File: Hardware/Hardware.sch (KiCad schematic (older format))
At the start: 65 parts

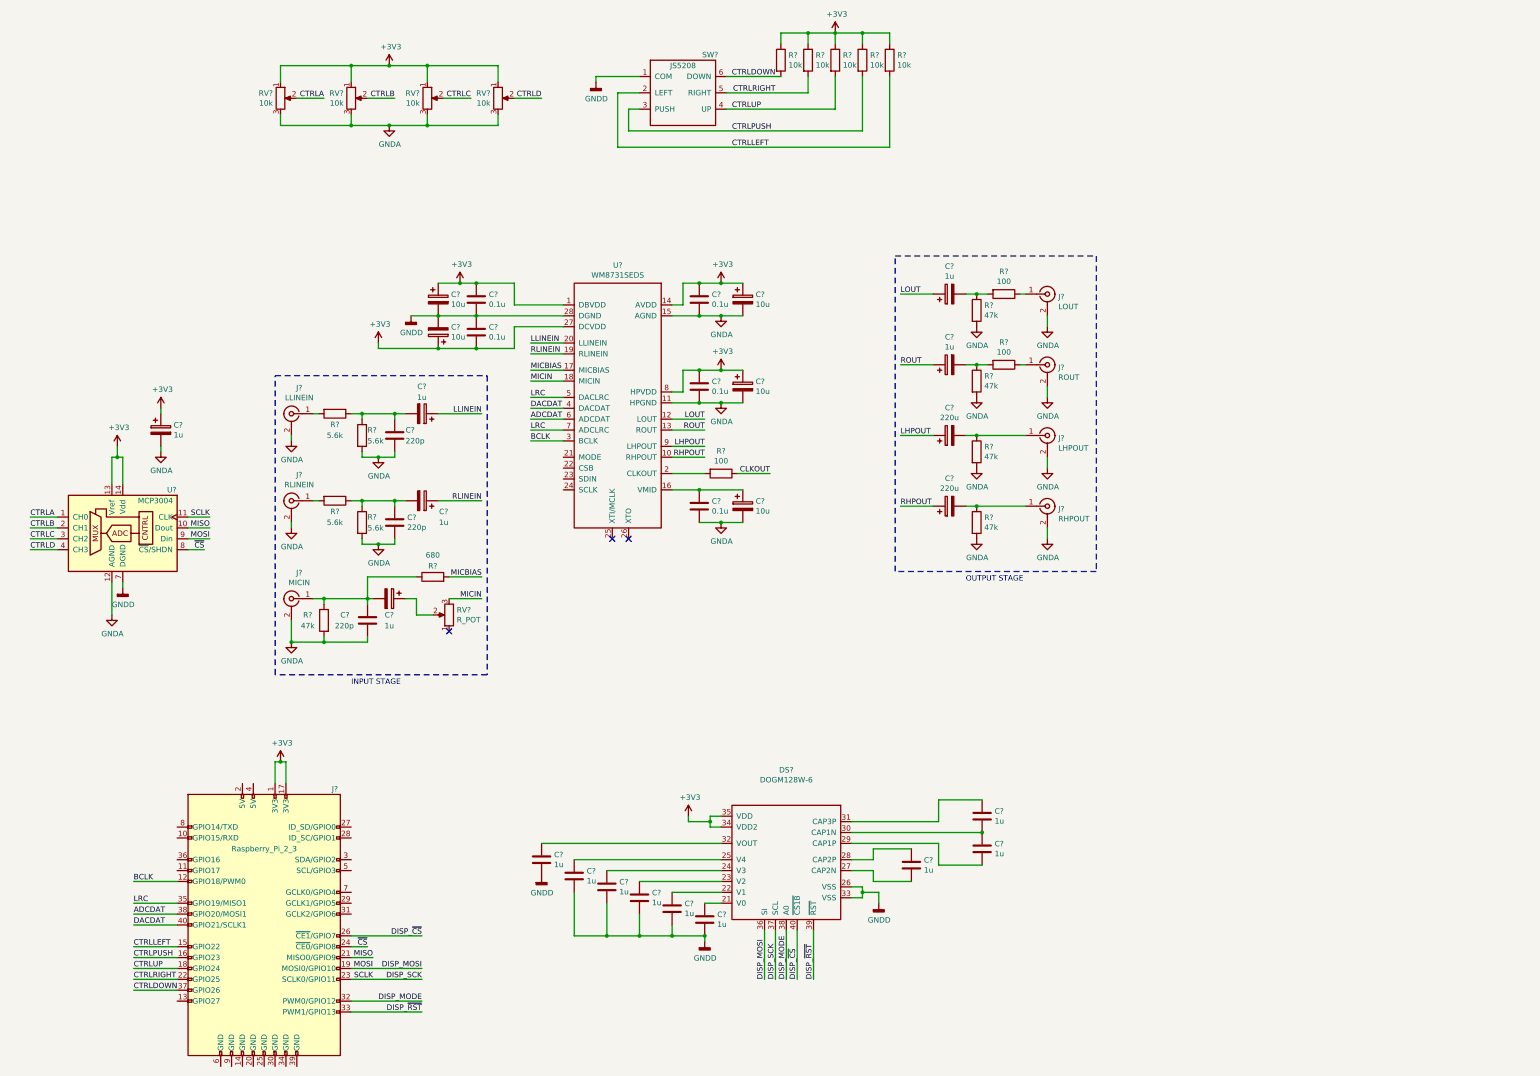
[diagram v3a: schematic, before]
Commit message: Organised schematic sheet
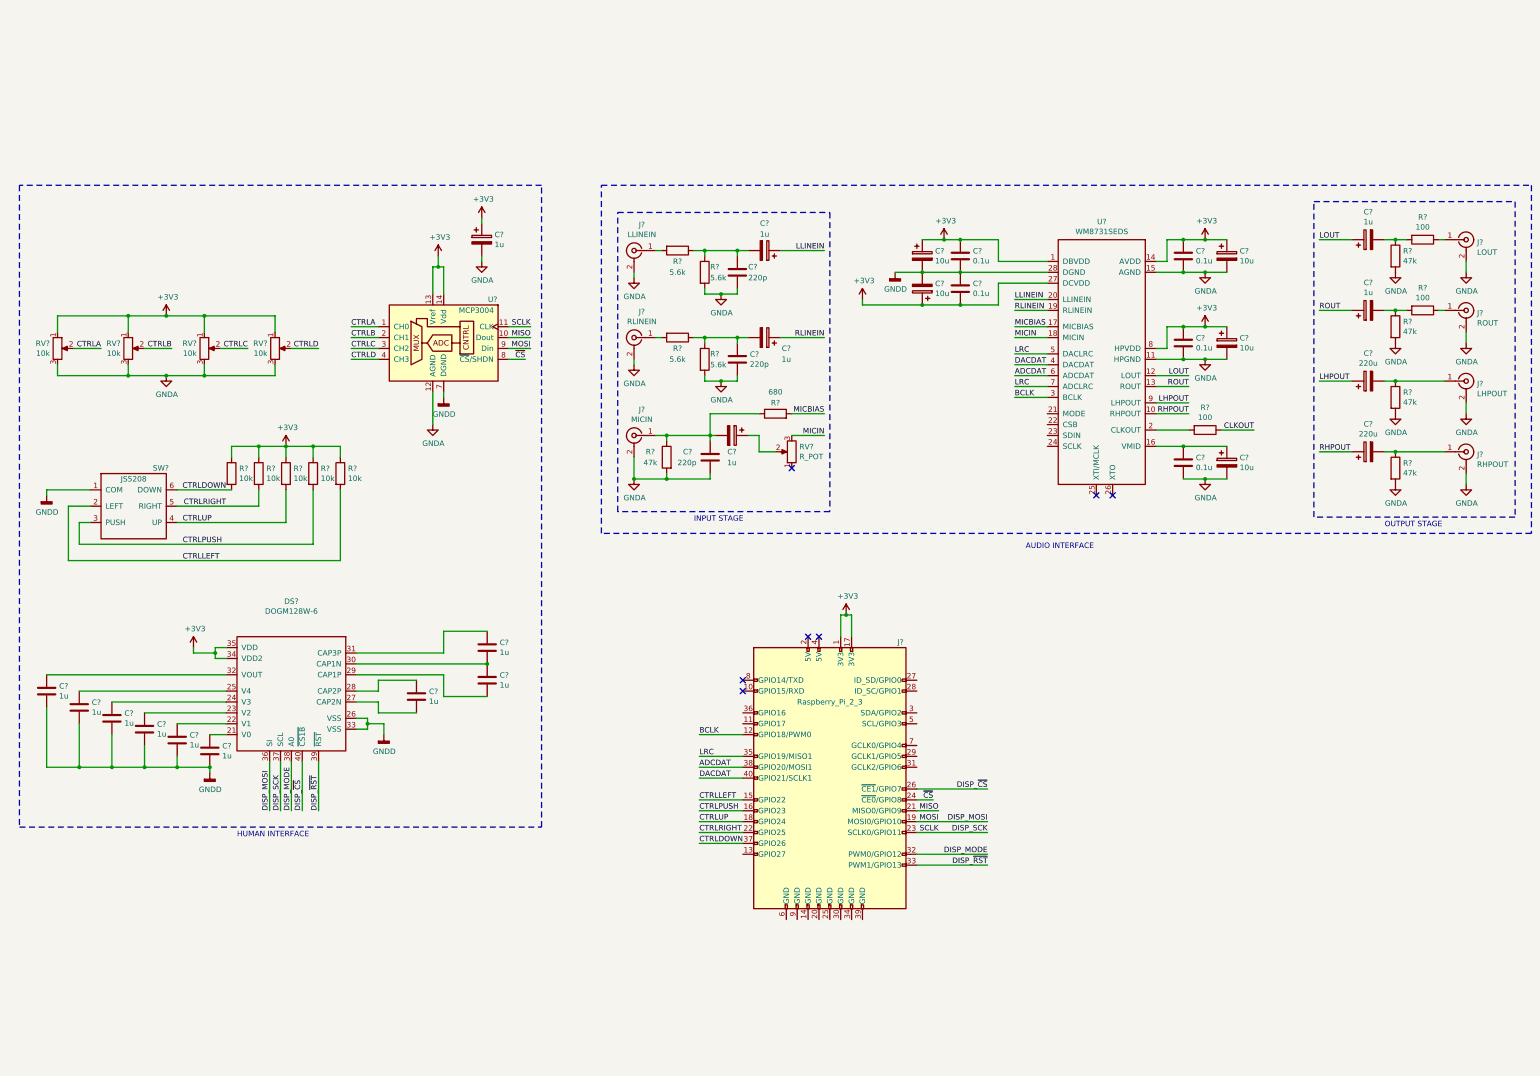
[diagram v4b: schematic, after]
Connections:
- no-connect marks 3 -> 7
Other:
- note added: "AUDIO INTERFACE"
- note added: "HUMAN INTERFACE"
- moved on the sheet: C?, DS?, J?, R?, RV?, SW?, U?

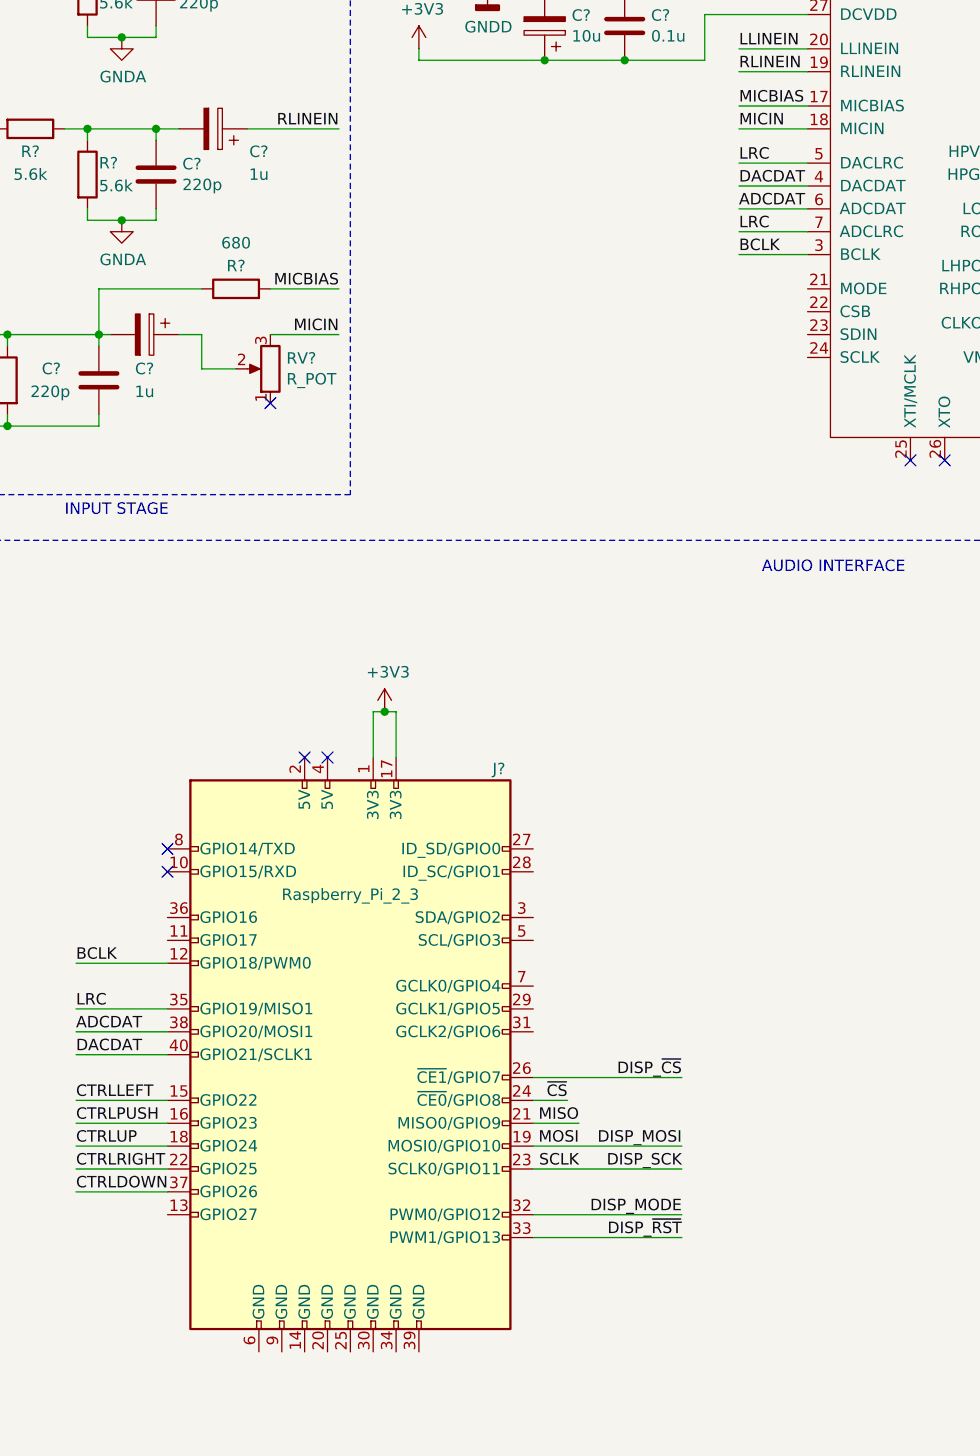
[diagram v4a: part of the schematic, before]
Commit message: Connected WM8731SEDS control interface through i2c to Raspberry Pi, finished connection of all systems
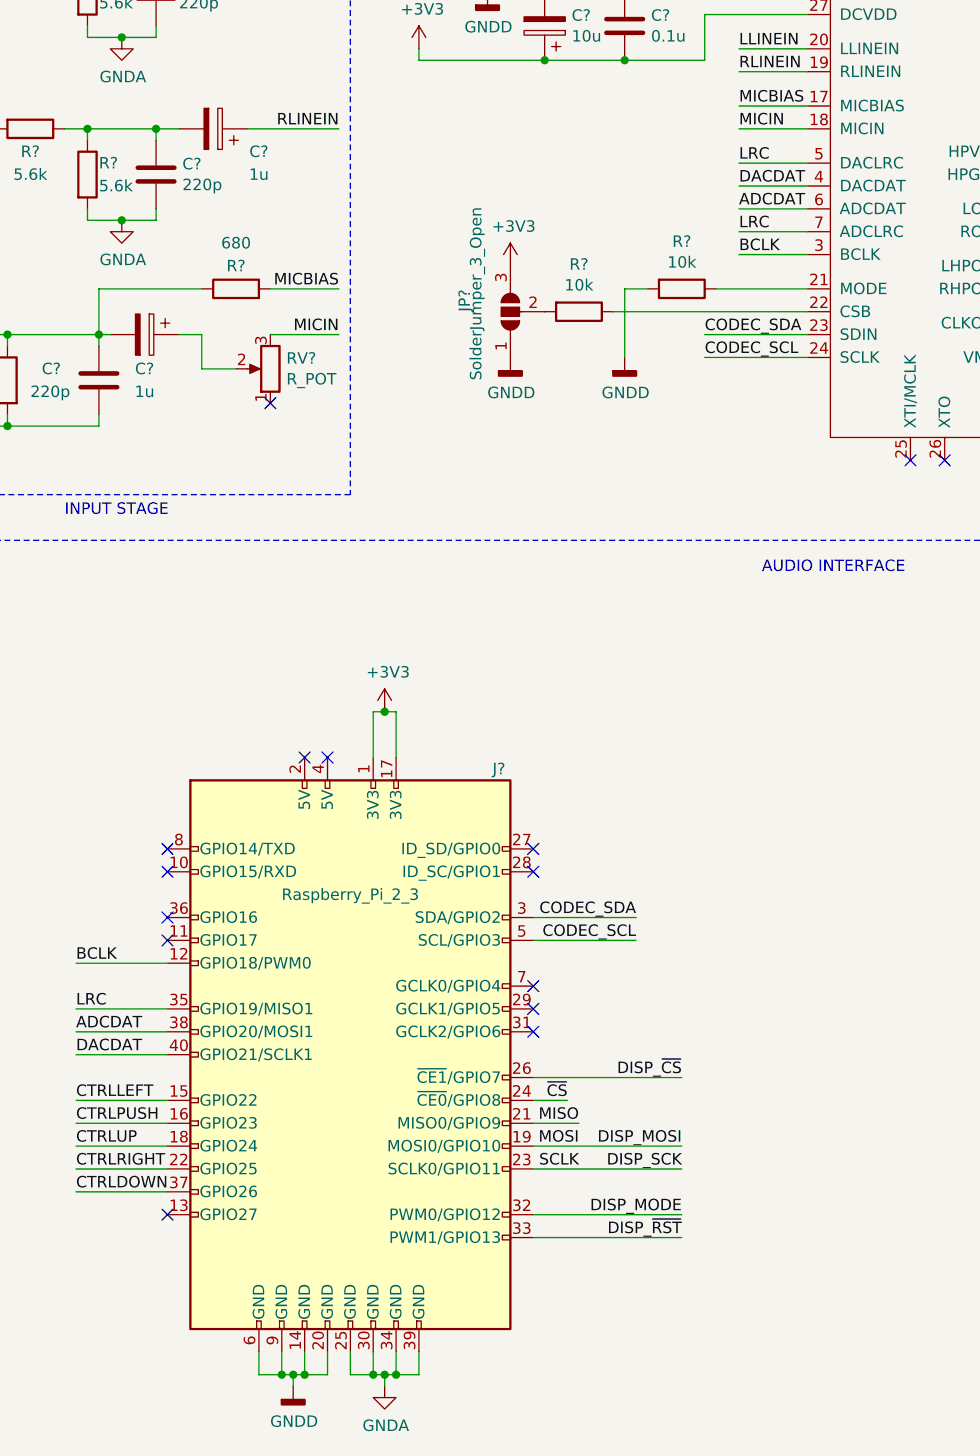
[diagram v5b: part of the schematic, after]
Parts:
- added JP?: SolderJumper_3_Open, symbol Jumper:SolderJumper_3_Open
- added R? (x2): 10k, symbol Device:R
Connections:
- net +3V3: now also JP?.3 (B)
- net GNDA: now also J?.25 (GND), J?.30 (GND), J?.34 (GND), J?.39 (GND)
- net GNDD: now also J?.14 (GND), J?.20 (GND), J?.6 (GND), J?.9 (GND), JP?.1 (A), R?.2
- net CODEC_SDA: now reaches J?.3 (SDA/GPIO2)
- net CODEC_SDA: now also U?.23 (SDIN)
- net CODEC_SCL: now reaches J?.5 (SCL/GPIO3)
- net CODEC_SCL: now also U?.24 (SCLK)
- net at U?.21 (MODE): now also R?.1
- net at U?.22 (CSB): now also R?.1
- new net: JP?.2 (C), R?.2
- no-connect marks 7 -> 15
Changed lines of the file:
@@
 encoding utf-8
 Sheet 1 1
-Title ""
-Date ""
-Rev ""
-Comp ""
+Title "signl main"
+Date "2020-02-18"
+Rev "1.0"
+Comp "signl"
 Comment1 ""
 Comment2 ""
@@
 NoConn ~ 7550 6800
 NoConn ~ 7550 6900
+$Comp
+L Device:R R?
+U 1 1 5E4D012A
+P 9350 4450
+F 0 "R?" V 9143 4450 50  0000 C CNN
+F 1 "10k" V 9234 4450 50  0000 C CNN
+F 2 "" V 9280 4450 50  0001 C CNN
+F 3 "~" H 9350 4450 50  0001 C CNN
+	1    9350 4450
+	0    1    1    0
+$EndComp
+$Comp
+L Jumper:SolderJumper_3_Open JP?
+U 1 1 5E4D0C03
+P 9050 4450
+F 0 "JP?" H 9050 4650 50  0000 L CNN
+F 1 "SolderJumper_3_Open" H 8750 4600 50  0000 L CNN
+F 2 "" H 9050 4450 50  0001 C CNN
+F 3 "~" H 9050 4450 50  0001 C CNN
+	1    9050 4450
+	0    -1   -1   0
+$EndComp
+Wire Wire Line
+	9500 4450 10350 4450
+$Comp
+L power:+3V3 #PWR?
+U 1 1 5E4E3D4A
+P 9050 4250
+F 0 "#PWR?" H 9050 4100 50  0001 C CNN
+F 1 "+3V3" H 9065 4423 50  0000 C CNN
+F 2 "" H 9050 4250 50  0001 C CNN
+F 3 "" H 9050 4250 50  0001 C CNN
+	1    9050 4250
+	1    0    0    -1
+$EndComp
+$Comp
+L power:GNDD #PWR?
+U 1 1 5E4E4370
+P 9050 4650
+F 0 "#PWR?" H 9050 4400 50  0001 C CNN
+F 1 "GNDD" H 9054 4495 50  0000 C CNN
+F 2 "" H 9050 4650 50  0001 C CNN
+F 3 "" H 9050 4650 50  0001 C CNN
+	1    9050 4650
+	1    0    0    -1
+$EndComp
+$Comp
+L Device:R R?
+U 1 1 5E4E4813
+P 9800 4350
+F 0 "R?" V 9593 4350 50  0000 C CNN
+F 1 "10k" V 9684 4350 50  0000 C CNN
+F 2 "" V 9730 4350 50  0001 C CNN
+F 3 "~" H 9800 4350 50  0001 C CNN
+	1    9800 4350
+	0    1    1    0
+$EndComp
+Wire Wire Line
+	9950 4350 10350 4350
+Wire Wire Line
+	9650 4350 9550 4350
+Wire Wire Line
+	9550 4350 9550 4650
+$Comp
+L power:GNDD #PWR?
+U 1 1 5E54E244
+P 9550 4650
+F 0 "#PWR?" H 9550 4400 50  0001 C CNN
+F 1 "GNDD" H 9554 4495 50  0000 C CNN
+F 2 "" H 9550 4650 50  0001 C CNN
+F 3 "" H 9550 4650 50  0001 C CNN
+	1    9550 4650
+	1    0    0    -1
+$EndComp
+Text Label 9900 4550 0    50   ~ 0
+CODEC_SDA
+Wire Wire Line
+	9900 4550 10350 4550
+Text Label 9900 4650 0    50   ~ 0
+CODEC_SCL
+Wire Wire Line
+	9900 4650 10350 4650
+Text Label 9600 7100 2    50   ~ 0
+CODEC_SDA
+Wire Wire Line
+	9600 7100 9150 7100
+Text Label 9600 7200 2    50   ~ 0
+CODEC_SCL
+Wire Wire Line
+	9600 7200 9150 7200
+NoConn ~ 9150 6800
+NoConn ~ 9150 6900
+NoConn ~ 9150 7400
+NoConn ~ 9150 7500
+NoConn ~ 9150 7600
+NoConn ~ 7550 7100
+NoConn ~ 7550 7200
+NoConn ~ 7550 8400
+$Comp
+L power:GNDD #PWR?
+U 1 1 5E647AB0
+P 8100 9150
+F 0 "#PWR?" H 8100 8900 50  0001 C CNN
+F 1 "GNDD" H 8104 8995 50  0000 C CNN
+F 2 "" H 8100 9150 50  0001 C CNN
+F 3 "" H 8100 9150 50  0001 C CNN
+	1    8100 9150
+	1    0    0    -1
+$EndComp
+Wire Wire Line
+	7950 9000 7950 9100
+Wire Wire Line
+	7950 9100 8050 9100
+Wire Wire Line
+	8250 9100 8250 9000
+Wire Wire Line
+	8150 9000 8150 9100
+Connection ~ 8150 9100
+Wire Wire Line
+	8150 9100 8250 9100
+Wire Wire Line
+	8050 9000 8050 9100
+Connection ~ 8050 9100
+Wire Wire Line
+	8050 9100 8100 9100
+Wire Wire Line
+	8100 9150 8100 9100
+Connection ~ 8100 9100
+Wire Wire Line
+	8100 9100 8150 9100
+$Comp
+L power:GNDA #PWR?
+U 1 1 5E6933D8
+P 8500 9150
+F 0 "#PWR?" H 8500 8900 50  0001 C CNN
+F 1 "GNDA" H 8505 8977 50  0000 C CNN
+F 2 "" H 8500 9150 50  0001 C CNN
+F 3 "" H 8500 9150 50  0001 C CNN
+	1    8500 9150
+	1    0    0    -1
+$EndComp
+Wire Wire Line
+	8500 9150 8500 9100
+Wire Wire Line
+	8500 9100 8450 9100
+Wire Wire Line
+	8350 9100 8350 9000
+Wire Wire Line
+	8450 9000 8450 9100
+Connection ~ 8450 9100
+Wire Wire Line
+	8450 9100 8350 9100
+Wire Wire Line
+	8550 9000 8550 9100
+Wire Wire Line
+	8550 9100 8500 9100
+Connection ~ 8500 9100
+Wire Wire Line
+	8650 9000 8650 9100
+Wire Wire Line
+	8650 9100 8550 9100
+Connection ~ 8550 9100
 $EndSCHEMATC
